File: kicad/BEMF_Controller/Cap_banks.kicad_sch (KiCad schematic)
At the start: 60 parts

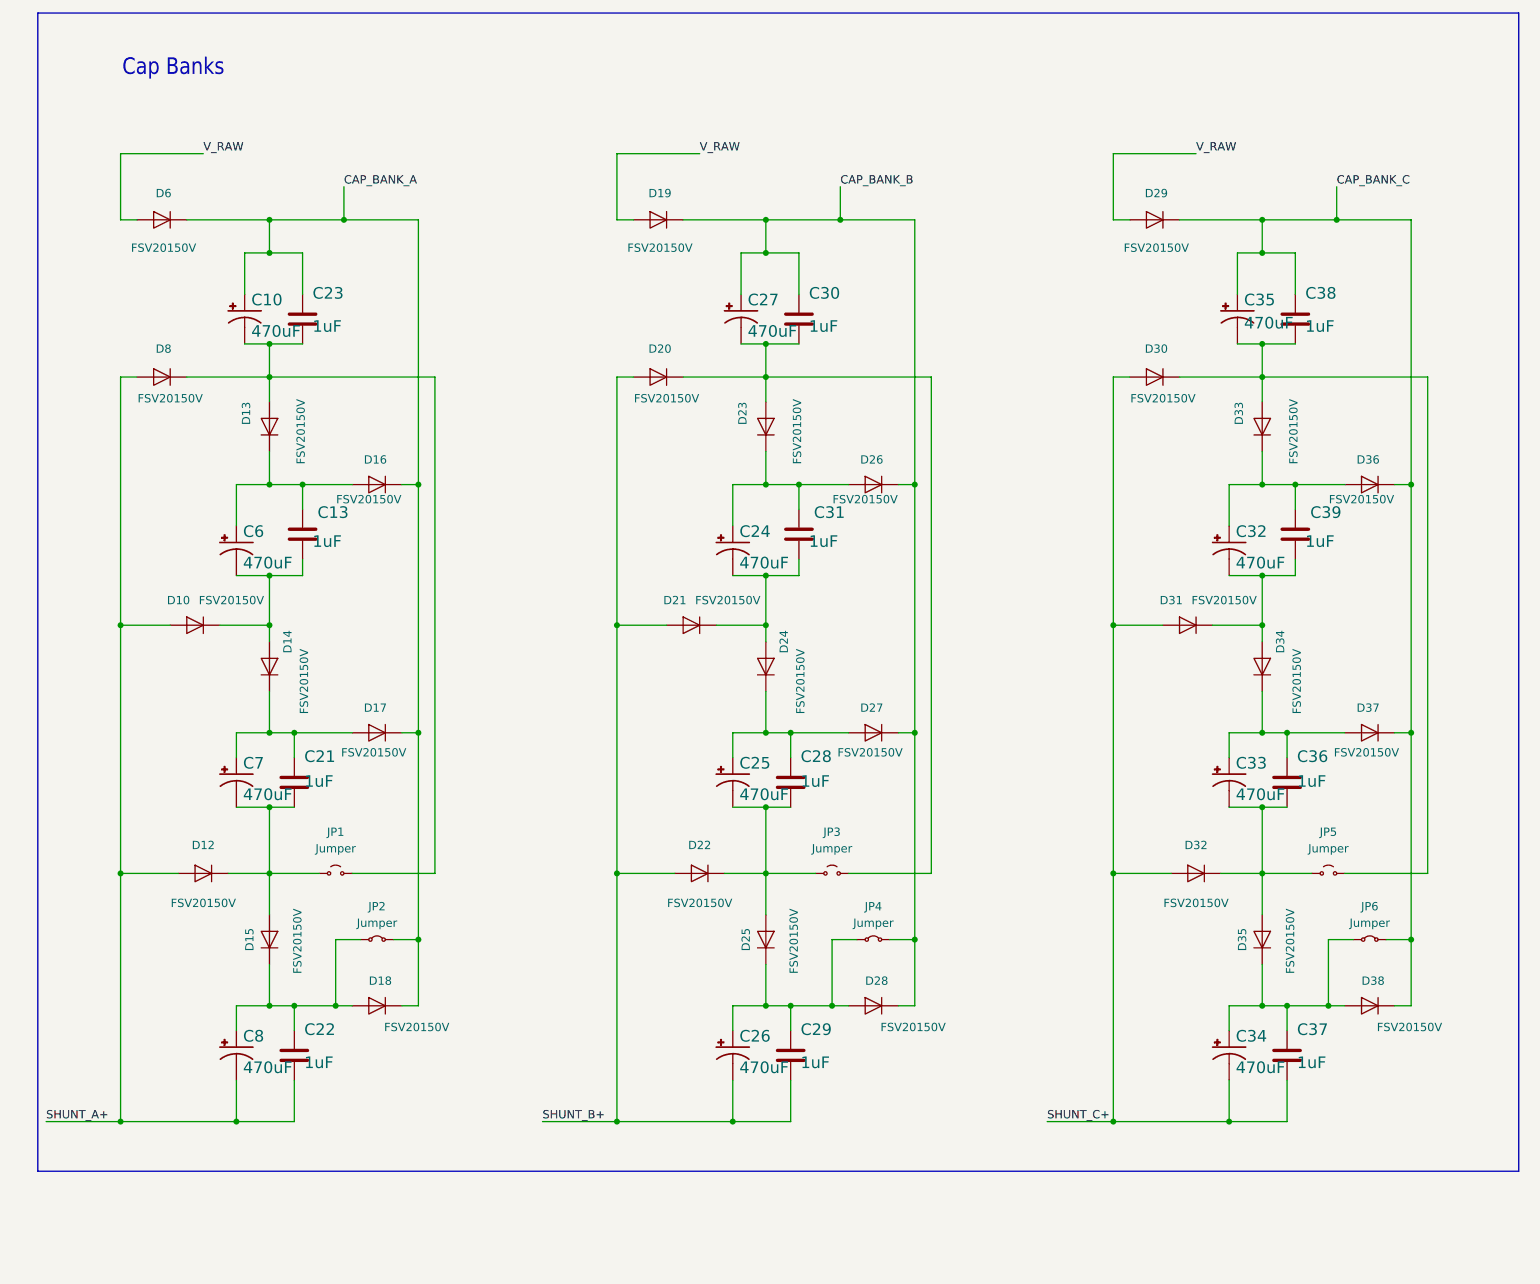
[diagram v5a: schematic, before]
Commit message: Several updates to analog section
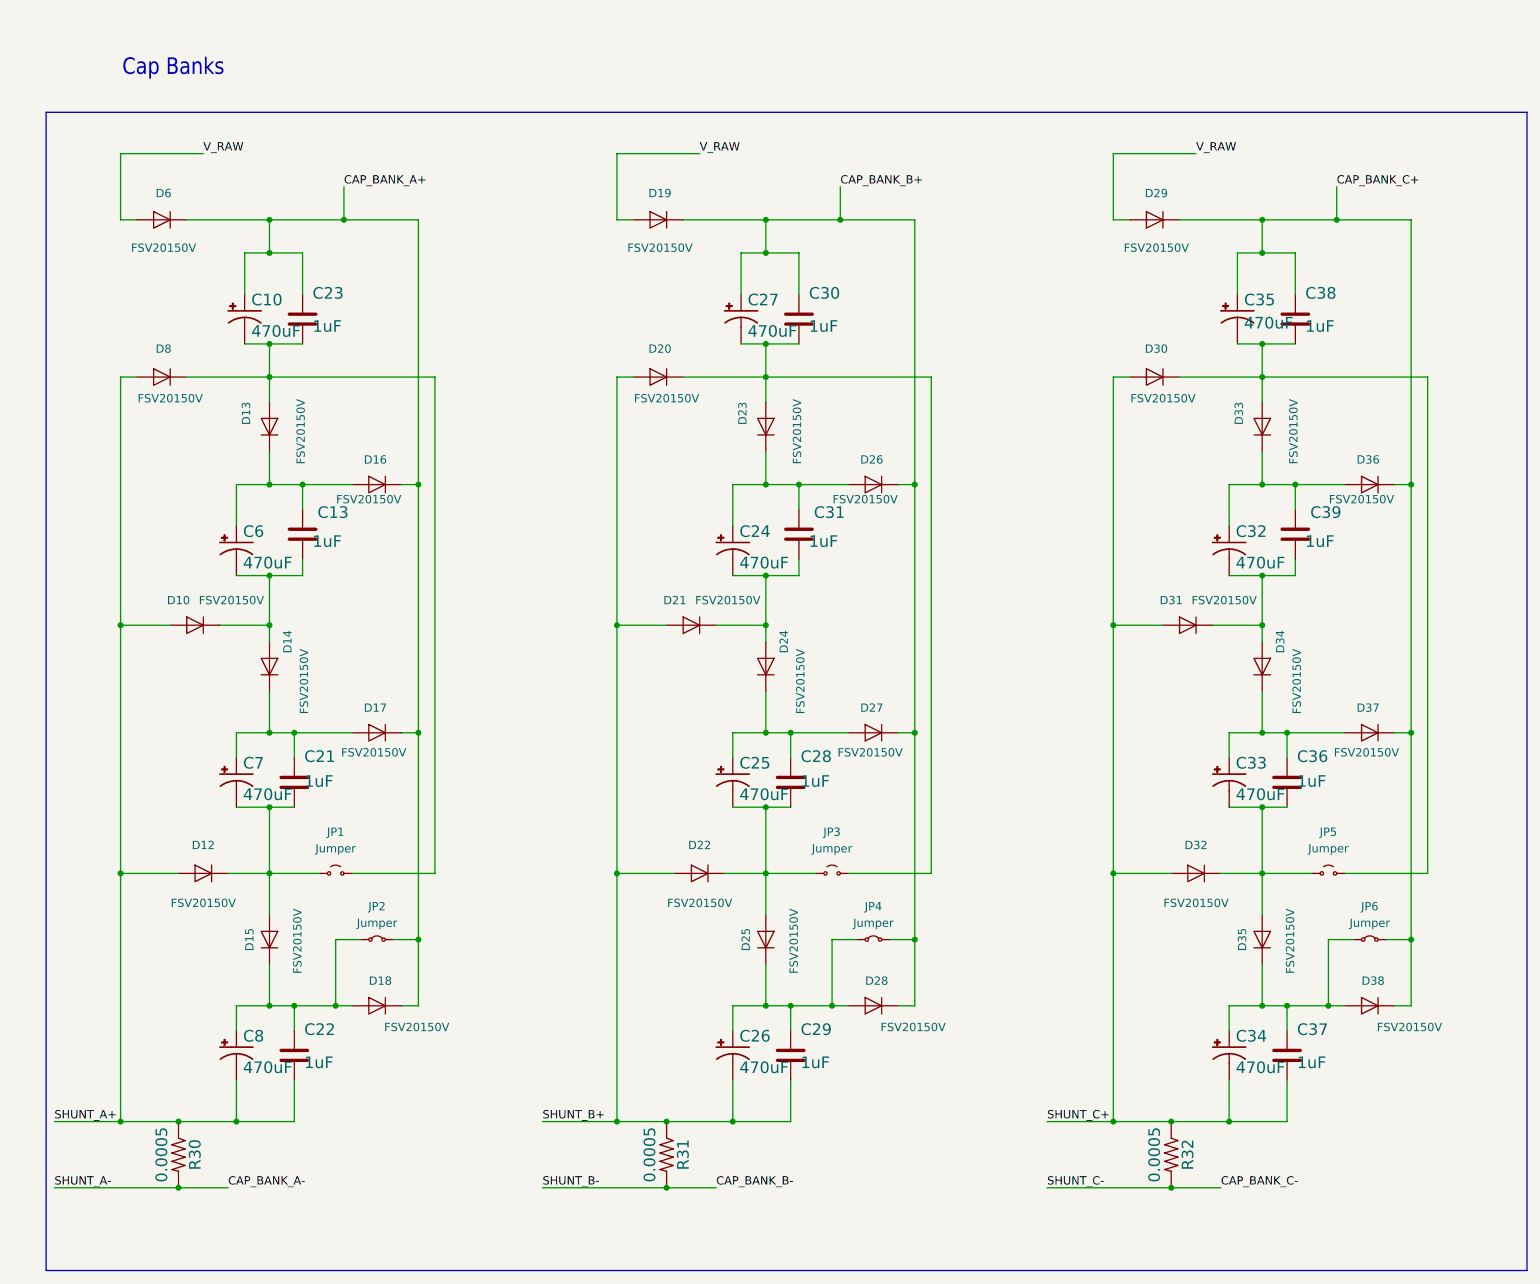
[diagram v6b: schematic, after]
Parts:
- added R30, R31, R32: 0.0005, main:R2512, symbol main-eagle-import:RESISTOR
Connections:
- net SHUNT_A+: now also R30.1
- net SHUNT_B+: now also R31.1
- net SHUNT_C+: now also R32.1
- net CAP_BANK_A renamed CAP_BANK_A+
- net CAP_BANK_B renamed CAP_BANK_B+
- net CAP_BANK_C renamed CAP_BANK_C+
- new net CAP_BANK_A-: R30.2
- new net CAP_BANK_B-: R31.2
- new net CAP_BANK_C-: R32.2

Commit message: First version of PCB layout.
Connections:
- net CAP_BANK_B- is gone; now on net CAP_BANK_GND: R31.2
- net CAP_BANK_C- is gone; now on net CAP_BANK_GND: R32.2
- net CAP_BANK_A- renamed CAP_BANK_GND
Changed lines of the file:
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@@
 		)
 	)
-	(label "SHUNT_B+"
+	(global_label "SHUNT_A-"
+		(shape input)
+		(at 11.43 185.42 0)
+		(fields_autoplaced yes)
+		(effects
+			(font
+				(size 1.27 1.27)
+			)
+			(justify left)
+		)
+		(property "Intersheetrefs" "${INTERSHEET_REFS}"
+			(at 24.2124 185.42 0)
+			(effects
+				(font
+					(size 1.27 1.27)
+				)
+				(justify left)
+				(hide yes)
+			)
+		)
+	)
+	(global_label "CAP_BANK_GND"
+		(shape input)
+		(at 190.5 185.42 0)
+		(fields_autoplaced yes)
+		(effects
+			(font
+				(size 1.27 1.27)
+			)
+			(justify left)
+		)
+		(property "Intersheetrefs" "${INTERSHEET_REFS}"
+			(at 207.8786 185.42 0)
+			(effects
+				(font
+					(size 1.27 1.27)
+				)
+				(justify left)
+				(hide yes)
+			)
+		)
+	)
+	(global_label "V_RAW"
+		(shape input)
+		(at 110.49 26.67 0)
+		(fields_autoplaced yes)
+		(effects
+			(font
+				(size 1.27 1.27)
+			)
+			(justify left)
+		)
+		(property "Intersheetrefs" "${INTERSHEET_REFS}"
+			(at 119.3414 26.67 0)
+			(effects
+				(font
+					(size 1.27 1.27)
+				)
+				(justify left)
+				(hide yes)
+			)
+		)
+	)
+	(global_label "SHUNT_B+"
+		(shape input)
 		(at 86.36 175.26 0)
 		(fields_autoplaced yes)
@@
 				(size 1.27 1.27)
 			)
-			(justify left bottom)
-		)
-	)
-	(label "CAP_BANK_C-"
-		(at 190.5 185.42 0)
-		(fields_autoplaced yes)
-		(effects
-			(font
-				(size 1.27 1.27)
-			)
-			(justify left bottom)
-		)
-	)
-	(label "V_RAW"
+			(justify left)
+		)
+		(property "Intersheetrefs" "${INTERSHEET_REFS}"
+			(at 99.3238 175.26 0)
+			(effects
+				(font
+					(size 1.27 1.27)
+				)
+				(justify left)
+				(hide yes)
+			)
+		)
+	)
+	(global_label "V_RAW"
+		(shape input)
+		(at 34.29 26.67 0)
+		(fields_autoplaced yes)
+		(effects
+			(font
+				(size 1.27 1.27)
+			)
+			(justify left)
+		)
+		(property "Intersheetrefs" "${INTERSHEET_REFS}"
+			(at 43.1414 26.67 0)
+			(effects
+				(font
+					(size 1.27 1.27)
+				)
+				(justify left)
+				(hide yes)
+			)
+		)
+	)
+	(global_label "CAP_BANK_B+"
+		(shape input)
+		(at 132.08 31.75 0)
+		(fields_autoplaced yes)
+		(effects
+			(font
+				(size 1.27 1.27)
+			)
+			(justify left)
+		)
+		(property "Intersheetrefs" "${INTERSHEET_REFS}"
+			(at 148.4305 31.75 0)
+			(effects
+				(font
+					(size 1.27 1.27)
+				)
+				(justify left)
+				(hide yes)
+			)
+		)
+	)
+	(global_label "CAP_BANK_A+"
+		(shape input)
+		(at 55.88 31.75 0)
+		(fields_autoplaced yes)
+		(effects
+			(font
+				(size 1.27 1.27)
+			)
+			(justify left)
+		)
+		(property "Intersheetrefs" "${INTERSHEET_REFS}"
+			(at 72.0491 31.75 0)
+			(effects
+				(font
+					(size 1.27 1.27)
+				)
+				(justify left)
+				(hide yes)
+			)
+		)
+	)
+	(global_label "CAP_BANK_C+"
+		(shape input)
+		(at 208.28 31.75 0)
+		(fields_autoplaced yes)
+		(effects
+			(font
+				(size 1.27 1.27)
+			)
+			(justify left)
+		)
+		(property "Intersheetrefs" "${INTERSHEET_REFS}"
+			(at 224.6305 31.75 0)
+			(effects
+				(font
+					(size 1.27 1.27)
+				)
+				(justify left)
+				(hide yes)
+			)
+		)
+	)
+	(global_label "CAP_BANK_GND"
+		(shape input)
+		(at 38.1 185.42 0)
+		(fields_autoplaced yes)
+		(effects
+			(font
+				(size 1.27 1.27)
+			)
+			(justify left)
+		)
+		(property "Intersheetrefs" "${INTERSHEET_REFS}"
+			(at 55.4786 185.42 0)
+			(effects
+				(font
+					(size 1.27 1.27)
+				)
+				(justify left)
+				(hide yes)
+			)
+		)
+	)
+	(global_label "SHUNT_C-"
+		(shape input)
+		(at 163.83 185.42 0)
+		(fields_autoplaced yes)
+		(effects
+			(font
+				(size 1.27 1.27)
+			)
+			(justify left)
+		)
+		(property "Intersheetrefs" "${INTERSHEET_REFS}"
+			(at 176.7938 185.42 0)
+			(effects
+				(font
+					(size 1.27 1.27)
+				)
+				(justify left)
+				(hide yes)
+			)
+		)
+	)
+	(global_label "SHUNT_B-"
+		(shape input)
+		(at 86.36 185.42 0)
+		(fields_autoplaced yes)
+		(effects
+			(font
+				(size 1.27 1.27)
+			)
+			(justify left)
+		)
+		(property "Intersheetrefs" "${INTERSHEET_REFS}"
+			(at 99.3238 185.42 0)
+			(effects
+				(font
+					(size 1.27 1.27)
+				)
+				(justify left)
+				(hide yes)
+			)
+		)
+	)
+	(global_label "SHUNT_C+"
+		(shape input)
+		(at 163.83 175.26 0)
+		(fields_autoplaced yes)
+		(effects
+			(font
+				(size 1.27 1.27)
+			)
+			(justify left)
+		)
+		(property "Intersheetrefs" "${INTERSHEET_REFS}"
+			(at 176.7938 175.26 0)
+			(effects
+				(font
+					(size 1.27 1.27)
+				)
+				(justify left)
+				(hide yes)
+			)
+		)
+	)
+	(global_label "SHUNT_A+"
+		(shape input)
+		(at 11.43 175.26 0)
+		(fields_autoplaced yes)
+		(effects
+			(font
+				(size 1.27 1.27)
+			)
+			(justify left)
+		)
+		(property "Intersheetrefs" "${INTERSHEET_REFS}"
+			(at 24.2124 175.26 0)
+			(effects
+				(font
+					(size 1.27 1.27)
+				)
+				(justify left)
+				(hide yes)
+			)
+		)
+	)
+	(global_label "CAP_BANK_GND"
+		(shape input)
+		(at 113.03 185.42 0)
+		(fields_autoplaced yes)
+		(effects
+			(font
+				(size 1.27 1.27)
+			)
+			(justify left)
+		)
+		(property "Intersheetrefs" "${INTERSHEET_REFS}"
+			(at 130.4086 185.42 0)
+			(effects
+				(font
+					(size 1.27 1.27)
+				)
+				(justify left)
+				(hide yes)
+			)
+		)
+	)
+	(global_label "V_RAW"
+		(shape input)
 		(at 186.69 26.67 0)
 		(fields_autoplaced yes)
@@
 				(size 1.27 1.27)
 			)
-			(justify left bottom)
-		)
-	)
-	(label "SHUNT_C-"
-		(at 163.83 185.42 0)
-		(fields_autoplaced yes)
-		(effects
-			(font
-				(size 1.27 1.27)
-			)
-			(justify left bottom)
-		)
-	)
-	(label "CAP_BANK_B-"
-		(at 113.03 185.42 0)
-		(fields_autoplaced yes)
-		(effects
-			(font
-				(size 1.27 1.27)
-			)
-			(justify left bottom)
-		)
-	)
-	(label "SHUNT_C+"
-		(at 163.83 175.26 0)
-		(fields_autoplaced yes)
-		(effects
-			(font
-				(size 1.27 1.27)
-			)
-			(justify left bottom)
-		)
-	)
-	(label "CAP_BANK_B+"
-		(at 132.08 31.75 0)
-		(fields_autoplaced yes)
-		(effects
-			(font
-				(size 1.27 1.27)
-			)
-			(justify left bottom)
-		)
-	)
-	(label "CAP_BANK_A+"
-		(at 55.88 31.75 0)
-		(fields_autoplaced yes)
-		(effects
-			(font
-				(size 1.27 1.27)
-			)
-			(justify left bottom)
-		)
-	)
-	(label "V_RAW"
-		(at 110.49 26.67 0)
-		(fields_autoplaced yes)
-		(effects
-			(font
-				(size 1.27 1.27)
-			)
-			(justify left bottom)
-		)
-	)
-	(label "CAP_BANK_C+"
-		(at 208.28 31.75 0)
-		(fields_autoplaced yes)
-		(effects
-			(font
-				(size 1.27 1.27)
-			)
-			(justify left bottom)
-		)
-	)
-	(label "V_RAW"
-		(at 34.29 26.67 0)
-		(fields_autoplaced yes)
-		(effects
-			(font
-				(size 1.27 1.27)
-			)
-			(justify left bottom)
-		)
-	)
-	(label "SHUNT_A-"
-		(at 11.43 185.42 0)
-		(fields_autoplaced yes)
-		(effects
-			(font
-				(size 1.27 1.27)
-			)
-			(justify left bottom)
-		)
-	)
-	(label "CAP_BANK_A-"
-		(at 38.1 185.42 0)
-		(fields_autoplaced yes)
-		(effects
-			(font
-				(size 1.27 1.27)
-			)
-			(justify left bottom)
-		)
-	)
-	(label "SHUNT_A+"
-		(at 11.43 175.26 0)
-		(fields_autoplaced yes)
-		(effects
-			(font
-				(size 1.27 1.27)
-			)
-			(justify left bottom)
-		)
-	)
-	(label "SHUNT_B-"
-		(at 86.36 185.42 0)
-		(fields_autoplaced yes)
-		(effects
-			(font
-				(size 1.27 1.27)
-			)
-			(justify left bottom)
-		)
-	)
+			(justify left)
+		)
+		(property "Intersheetrefs" "${INTERSHEET_REFS}"
+			(at 195.5414 26.67 0)
+			(effects
+				(font
+					(size 1.27 1.27)
+				)
+				(justify left)
+				(hide yes)
+			)
+		)
+	)
